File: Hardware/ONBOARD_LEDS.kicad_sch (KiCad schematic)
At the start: 38 parts, among them U10 74HC594, U9 74HC594

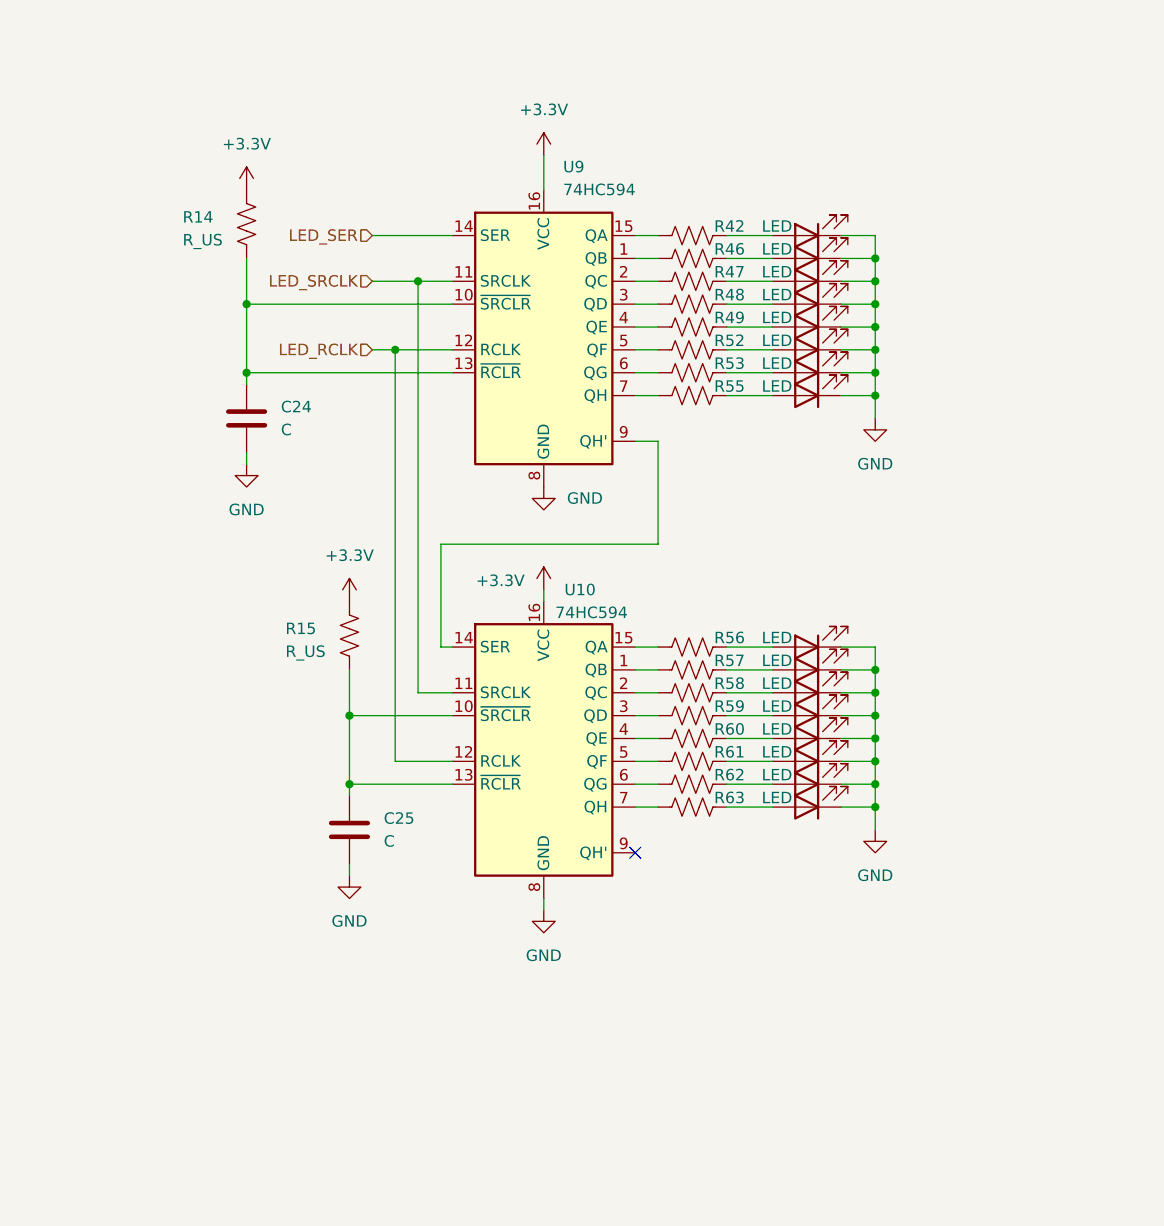
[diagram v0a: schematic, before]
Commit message: Confirmed ESP pin UART Boot-capability, labeled LED's, Moved Power sheet to a nicer location
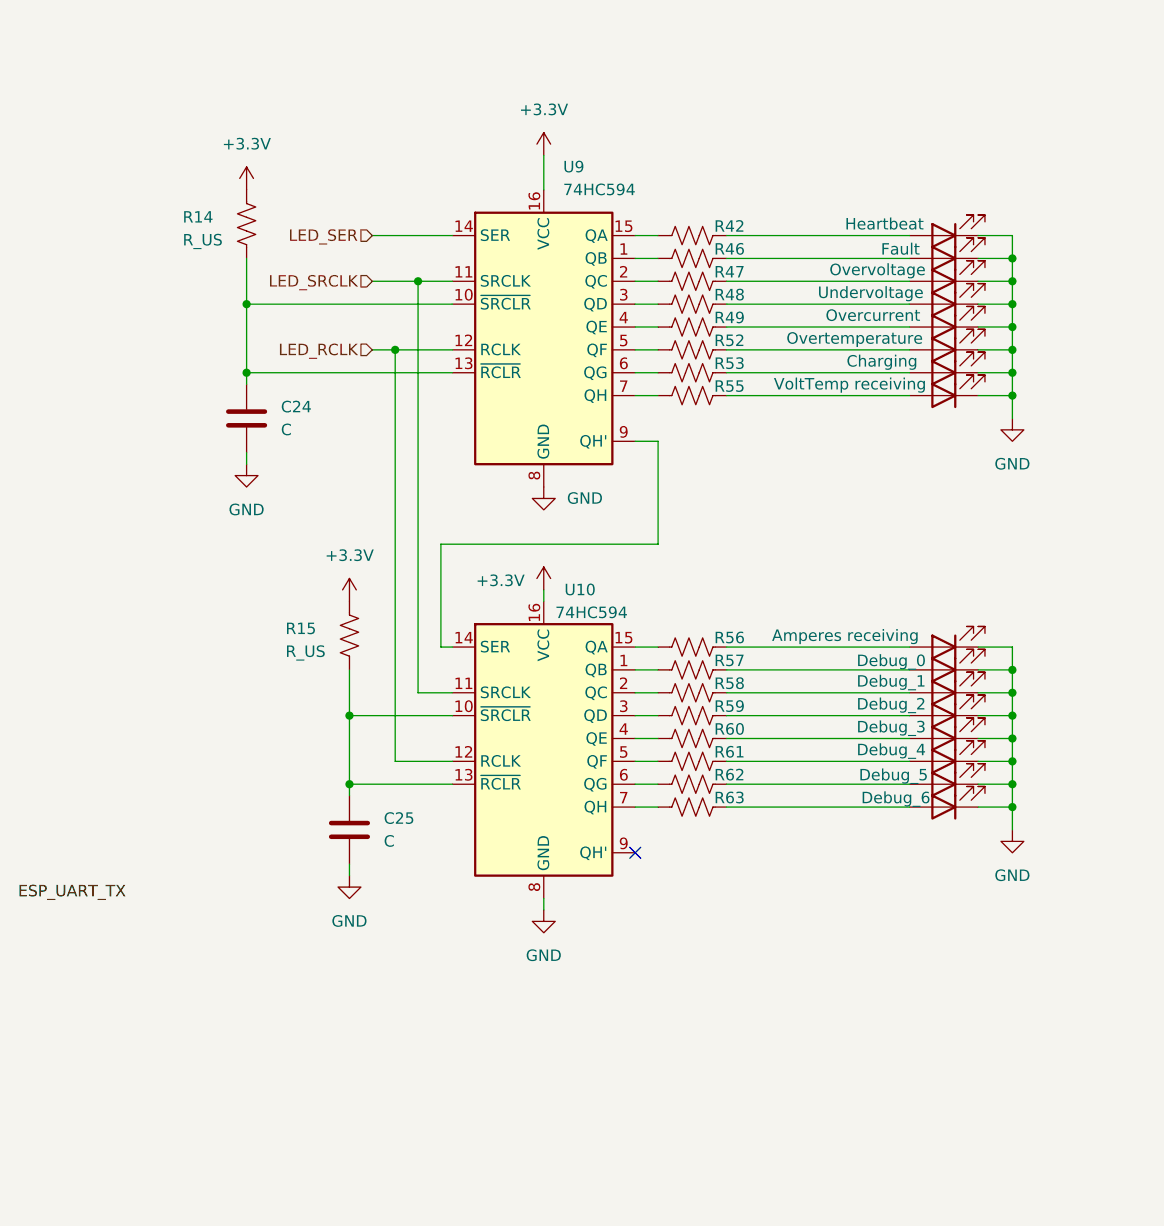
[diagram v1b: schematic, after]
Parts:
- D10: value LED -> Heartbeat
- D12: value LED -> Fault
- D13: value LED -> Overvoltage
- D14: value LED -> Undervoltage
- D15: value LED -> Overcurrent
- D16: value LED -> Overtemperature
- D17: value LED -> Charging
- D18: value LED -> VoltTemp receiving
- D19: value LED -> Amperes receiving
- D20: value LED -> Debug_0
- D21: value LED -> Debug_1
- D22: value LED -> Debug_2
- D23: value LED -> Debug_3
- D24: value LED -> Debug_4
- D25: value LED -> Debug_5
- D26: value LED -> Debug_6

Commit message: added fuse, made kiCad Sharepoint a submodule, added a pulldown, added test-points
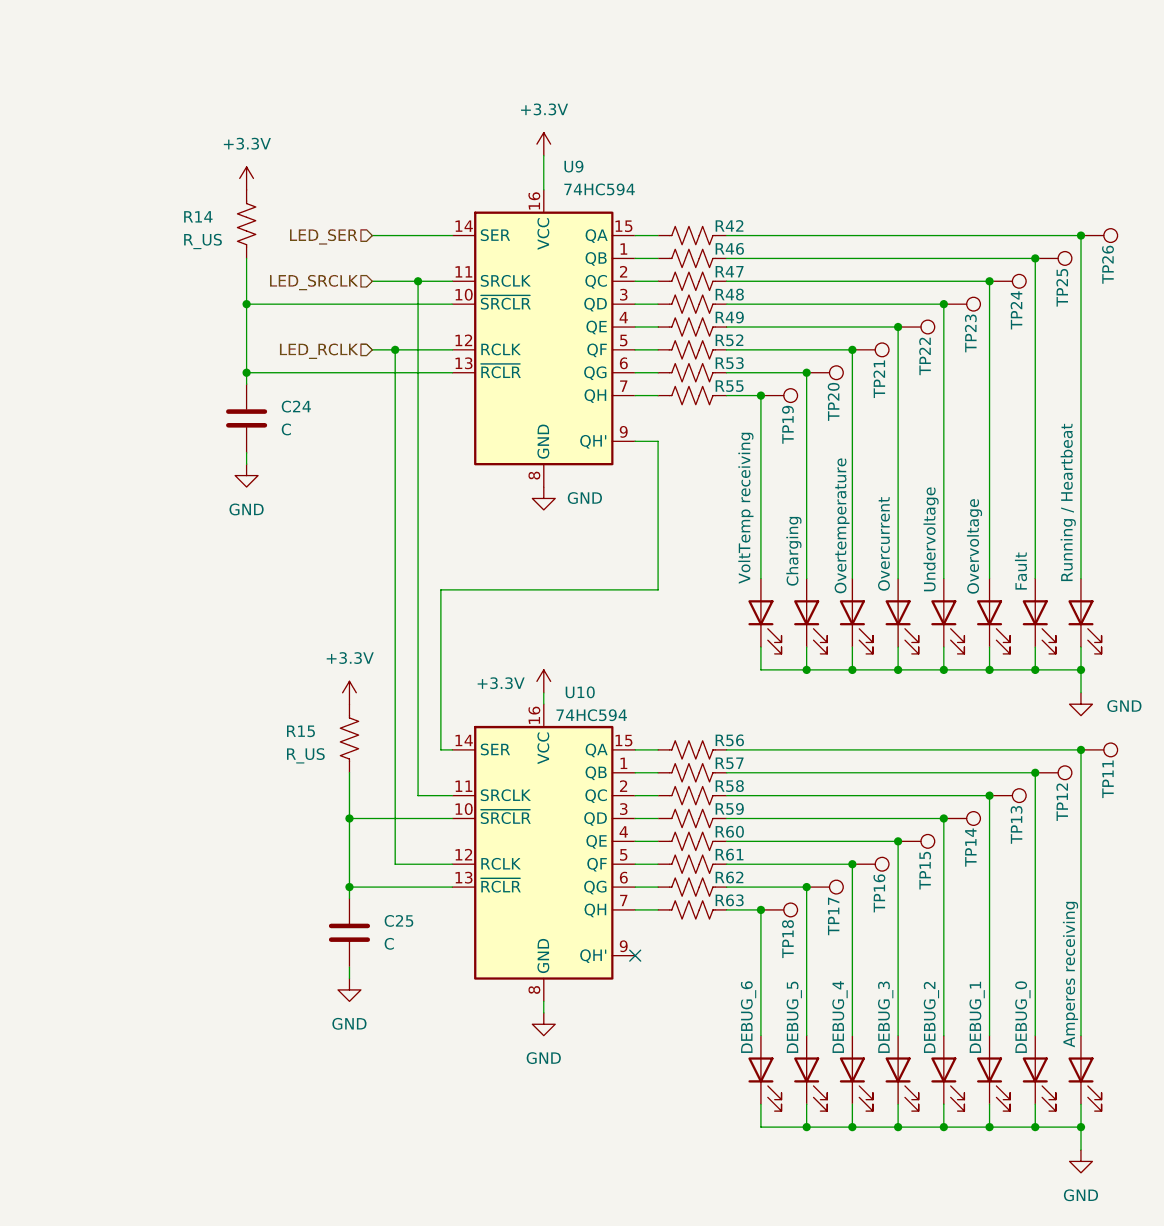
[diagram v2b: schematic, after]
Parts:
- removed D10: Heartbeat, symbol Device:LED
- removed D12: Fault, symbol Device:LED
- removed D13: Overvoltage, symbol Device:LED
- removed D14: Undervoltage, symbol Device:LED
- removed D15: Overcurrent, symbol Device:LED
- removed D16: Overtemperature, symbol Device:LED
- removed D17: Charging, symbol Device:LED
- removed D18: VoltTemp receiving, symbol Device:LED
- added D28: VoltTemp receiving, symbol Device:LED
- added D29: Charging, symbol Device:LED
- added D30: Overtemperature, symbol Device:LED
- added D31: Overcurrent, symbol Device:LED
- added D32: Undervoltage, symbol Device:LED
- added D33: Overvoltage, symbol Device:LED
- added D34: Fault, symbol Device:LED
- added D35: Running / Heartbeat, symbol Device:LED
- added TP11, TP12, TP13, TP14, TP15, TP16, TP17, TP18, TP19, TP20, TP21, TP22, TP23, TP24, TP25, TP26: TestPoint, symbol Connector:TestPoint
- D20: value Debug_0 -> DEBUG_0
- D21: value Debug_1 -> DEBUG_1
- D22: value Debug_2 -> DEBUG_2
- D23: value Debug_3 -> DEBUG_3
- D24: value Debug_4 -> DEBUG_4
- D25: value Debug_5 -> DEBUG_5
- D26: value Debug_6 -> DEBUG_6
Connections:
- net GND: now also D28.1 (K), D29.1 (K), D30.1 (K), D31.1 (K), D32.1 (K), D33.1 (K), D34.1 (K), D35.1 (K)
- net at R53.2: now also D29.2 (A), TP20.1
- net at D26.2 (A), R63.2: now also TP18.1
- net at R47.2: now also D33.2 (A), TP24.1
- net at D25.2 (A), R62.2: now also TP17.1
- net at D23.2 (A), R60.2: now also TP15.1
- net at R49.2: now also D31.2 (A), TP22.1
- net at R46.2: now also D34.2 (A), TP25.1
- net at D20.2 (A), R57.2: now also TP12.1
- net at D24.2 (A), R61.2: now also TP16.1
- net at R48.2: now also D32.2 (A), TP23.1
- net at R42.2: now also D35.2 (A), TP26.1
- net at D21.2 (A), R58.2: now also TP13.1
- net at D19.2 (A), R56.2: now also TP11.1
- net at D22.2 (A), R59.2: now also TP14.1
- net at R52.2: now also D30.2 (A), TP21.1
- net at R55.2: now also D28.2 (A), TP19.1
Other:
- moved on the sheet: C25, R15, R56, R57, R58, R59, R60, R61, R62, R63, U10

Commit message: Small tweaks
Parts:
- removed R14, R15: R_US, symbol Device:R_US
- added C34, C35: 0.1u, Capacitor_SMD:C_0603_1608Metric_Pad1.08x0.95mm_HandSolder, symbol Device:C
- added TP46: TestPoint, UTSVT_Special:TestPoint_HEX_3mmID, symbol Connector:TestPoint
- C24, C25: value C -> 0.1u; footprint (none) -> Capacitor_SMD:C_0603_1608Metric_Pad1.08x0.95mm_HandSolder
- D19, D20, D21, D22, D23, D24, D25, D26, D28, D29, D30, D31, D32, D33, D34, D35: footprint (none) -> LED_SMD:LED_0603_1608Metric
- R42, R46, R47, R48, R49, R52, R53, R55, R56, R57, R58, R59, R60, R61, R62, R63: footprint (none) -> Resistor_SMD:R_0603_1608Metric
- TP11, TP12, TP13, TP14, TP15, TP16, TP17, TP18, TP19, TP20, TP21, TP22, TP23, TP24, TP25, TP26: footprint (none) -> UTSVT_Special:TestPoint_HEX_3mmID
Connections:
- net +3.3V: now also C24.1, C25.1, U10.10 (~{SRCLR}), U10.13 (~{RCLR}), U9.10 (~{SRCLR}), U9.13 (~{RCLR}), C34.1, C35.1
- net GND: now also C34.2, C35.2
- net at U10.14 (SER), U9.9 (QH'): now also TP46.1

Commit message: Very, very intial layout designed. Many issues. Too bad!
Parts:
- removed TP11, TP12, TP13, TP14, TP15, TP16, TP17, TP18, TP19, TP20, TP21, TP22, TP23, TP24, TP25, TP26: TestPoint, UTSVT_Special:TestPoint_HEX_3mmID, symbol Connector:TestPoint
- AmpIn1: renamed from D19; value Amperes receiving -> AmpIn
- Chrging1: renamed from D29; value Charging -> Chrging
- Heart1: renamed from D35; value Running / Heartbeat -> Heart
- LowV1: renamed from D32; value Undervoltage -> LowV
- OverAmp1: renamed from D31; value Overcurrent -> OverAmp
- OverTemp1: renamed from D30; value Overtemperature -> OverTemp
- OverV1: renamed from D33; value Overvoltage -> OverV
- R42, R46, R47, R48, R49, R52, R53, R55, R57, R58, R59, R60, R61, R62, R63: value 120 -> 150
- TP46: footprint UTSVT_Special:TestPoint_HEX_3mmID -> TestPoint:TestPoint_Pad_1.0x1.0mm
- U10, U9: footprint (none) -> SN74HC594DWG4:SOIC127P1030X265-16N
- VTempIN1: renamed from D28; value VoltTemp receiving -> VTempIN
- renumbered D20 to DEBUG_0, D21 to DEBUG_1, D22 to DEBUG_2, D23 to DEBUG_3, D24 to DEBUG_4, D25 to DEBUG_5, D26 to DEBUG_6, D34 to Fault1

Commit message: Backup
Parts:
- U10, U9: value 74HC594 -> SN74HC594DWG4; footprint SN74HC594DWG4:SOIC127P1030X265-16N -> Shift Reg:SOIC127P1030X265-16N
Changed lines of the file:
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@@
 			)
 		)
-		(property "Value" "74HC594"
+		(property "Value" "SN74HC594DWG4"
 			(at 152.0033 45.72 0)
 			(effects
@@
 			)
 		)
-		(property "Footprint" "SN74HC594DWG4:SOIC127P1030X265-16N"
+		(property "Footprint" "Shift Reg:SOIC127P1030X265-16N"
 			(at 149.86 60.96 0)
 			(effects
@@
 			)
 		)
-		(property "Value" "74HC594"
+		(property "Value" "SN74HC594DWG4"
 			(at 151.13 104.14 0)
 			(effects
@@
 			)
 		)
-		(property "Footprint" "SN74HC594DWG4:SOIC127P1030X265-16N"
+		(property "Footprint" "Shift Reg:SOIC127P1030X265-16N"
 			(at 149.86 118.11 0)
 			(effects

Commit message: all 3d models added, minor fixes
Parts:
- removed TP46: TestPoint, TestPoint:TestPoint_Pad_1.0x1.0mm, symbol Connector:TestPoint
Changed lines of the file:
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@@
 	(paper "A4")
 	(junction
-		(at 162.56 82.55)
-		(diameter 0)
-		(color 0 0 0 0)
-	)
-	(junction
 		(at 179.07 149.86)
 		(diameter 0)
@@
 	(wire
 		(pts
-			(xy 162.56 85.09) (xy 162.56 82.55)
-		)
-		(stroke
-			(width 0)
-			(type default)
-		)
-	)
-	(wire
-		(pts
 			(xy 184.15 99.06) (xy 189.23 99.06)
 		)
@@
 					(unit 1)
 				)
-			)
-		)
-	)
-	(symbol
-		(lib_id "Connector:TestPoint")
-		(at 162.56 85.09 180)
-		(unit 1)
-		(exclude_from_sim no)
-		(in_bom yes)
-		(on_board yes)
-		(dnp no)
-		(property "Reference" "TP46"
-			(at 161.544 88.138 0)
-			(effects
-				(font
-					(size 1.27 1.27)
-				)
-				(justify left)
-			)
-		)
-		(property "Value" "TestPoint"
-			(at 160.02 87.1221 0)
-			(effects
-				(font
-					(size 1.27 1.27)
-				)
-				(justify left)
-				(hide yes)
-			)
-		)
-		(property "Footprint" "TestPoint:TestPoint_Pad_1.0x1.0mm"
-			(at 157.48 85.09 0)
-			(effects
-				(font
-					(size 1.27 1.27)
-				)
-				(hide yes)
-			)
-		)
-		(property "Datasheet" "~"
-			(at 157.48 85.09 0)
-			(effects
-				(font
-					(size 1.27 1.27)
-				)
-				(hide yes)
-			)
-		)
-		(property "Description" "test point"
-			(at 162.56 85.09 0)
-			(effects
-				(font
-					(size 1.27 1.27)
-				)
-				(hide yes)
-			)
-		)
-		(property "Manufactuerer" ""
-			(at 162.56 85.09 0)
-			(effects
-				(font
-					(size 1.27 1.27)
-				)
-				(hide yes)
-			)
-		)
-		(pin "1"
-		)
-		(instances
-			(project "BPS-Leader"
-				(path "/fb37da34-e420-4994-8cc1-079e8c0fa48e/ec328d6f-4db5-4eba-b704-0212808a8e56"
-					(reference "TP46")
-					(unit 1)
-				)

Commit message: small fixes
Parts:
- C24, C25, C34, C35: Manufactuerer (none) -> TAIYO YUDEN; P/N (none) -> MLASH168SB7104KTNA01
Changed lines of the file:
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@@
 			)
 		)
-		(property "Datasheet" "~"
+		(property "Datasheet" "https://ds.yuden.co.jp/TYCOMPAS/or/download?pn=MLAST063SCG681JFNA01&fileType=CA"
 			(at 116.84 71.12 0)
 			(effects
@@
 			)
 		)
-		(property "Manufactuerer" ""
+		(property "Manufactuerer" "TAIYO YUDEN "
+			(at 116.84 71.12 0)
+			(effects
+				(font
+					(size 1.27 1.27)
+				)
+				(hide yes)
+			)
+		)
+		(property "P/N" "MLASH168SB7104KTNA01 "
 			(at 116.84 71.12 0)
 			(effects
@@
 			)
 		)
-		(property "Datasheet" "~"
+		(property "Datasheet" "https://ds.yuden.co.jp/TYCOMPAS/or/download?pn=MLAST063SCG681JFNA01&fileType=CA"
 			(at 144.78 39.37 0)
 			(effects
@@
 			)
 		)
-		(property "Manufactuerer" ""
+		(property "Manufactuerer" "TAIYO YUDEN "
+			(at 144.78 39.37 0)
+			(effects
+				(font
+					(size 1.27 1.27)
+				)
+				(hide yes)
+			)
+		)
+		(property "P/N" "MLASH168SB7104KTNA01 "
 			(at 144.78 39.37 0)
 			(effects
@@
 			)
 		)
-		(property "Datasheet" "~"
+		(property "Datasheet" "https://ds.yuden.co.jp/TYCOMPAS/or/download?pn=MLAST063SCG681JFNA01&fileType=CA"
 			(at 128.27 128.27 0)
 			(effects
@@
 			)
 		)
-		(property "Manufactuerer" ""
+		(property "Manufactuerer" "TAIYO YUDEN "
+			(at 128.27 128.27 0)
+			(effects
+				(font
+					(size 1.27 1.27)
+				)
+				(hide yes)
+			)
+		)
+		(property "P/N" "MLASH168SB7104KTNA01 "
 			(at 128.27 128.27 0)
 			(effects
@@
 			)
 		)
-		(property "Datasheet" "~"
+		(property "Datasheet" "https://ds.yuden.co.jp/TYCOMPAS/or/download?pn=MLAST063SCG681JFNA01&fileType=CA"
 			(at 144.78 96.52 0)
 			(effects
@@
 			)
 		)
-		(property "Manufactuerer" ""
+		(property "Manufactuerer" "TAIYO YUDEN "
+			(at 144.78 96.52 0)
+			(effects
+				(font
+					(size 1.27 1.27)
+				)
+				(hide yes)
+			)
+		)
+		(property "P/N" "MLASH168SB7104KTNA01 "
 			(at 144.78 96.52 0)
 			(effects
